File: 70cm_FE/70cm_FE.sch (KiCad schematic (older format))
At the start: 150 parts, among them J2 U.FL, J3 U.FL, J4 U.FL, Q1 2SC3356, Q2 2SC3356, Q3 2SC3356, U1 HT7533-1, U2 74HC14, U3 74HC14, U4 LM393, U5 M68710L

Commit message: Add RF filtering details and other small additions
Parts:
- removed D1: SM4007PL, Diode_SMD:D_SOD-123F, symbol Device:D
- added C1, C2: 100p, Capacitor_SMD:C_0603_1608Metric, symbol Device:C
- added C15, C23: 10p, Capacitor_SMD:C_0603_1608Metric, symbol Device:C
- added C3: 4p7, Capacitor_SMD:C_0402_1005Metric, symbol Device:C
- added C5: DNP, Capacitor_SMD:C_0402_1005Metric, symbol Device:C
- added D1, D3: BAV99, Package_TO_SOT_SMD:SOT-23, symbol Diode:BAV99
- added H5, H6, H7, H8: Tooling hole, 70cm_FE:JLCPCB_ToolingHole, symbol Mechanical:MountingHole
- added JP4, JP7: ~, 70cm_FE:Jumper-3_0402, symbol 70cm_FE:Jumper_3_Bridged12
- added L1, L4: 15n, Inductor_SMD:L_0402_1005Metric, symbol Device:L
- added R1, R2, R26: 100k, Resistor_SMD:R_0402_1005Metric, symbol Device:R
- added R11, R13, R6, R7: DNP, Resistor_SMD:R_0402_1005Metric, symbol Device:R
- added R4: 47, Resistor_SMD:R_0402_1005Metric, symbol Device:R
- added R9: 0, Resistor_SMD:R_0402_1005Metric, symbol Device:R
- C7: renamed from C1; value 1p -> 4p7
- D8: renamed from D7; value BAT54C -> BAS70-05; LCSC (none) -> C77300 (extended)
- L12: renamed from L10; value 23 mm -> 22 mm
- L8: renamed from L7; value 24 mm -> 26 mm
- renumbered C8 to C10, C9 to C11, C14 to C13, C6 to C14, C17 to C16, C7 to C17, C19 to C18, C10 to C19, C11 to C20, C23 to C22, C13 to C24, C15 to C25, C16 to C26, C18 to C27, C25 to C28, C20 to C29, C31 to C30, C26 to C31, C22 to C32, C32 to C33, C28 to C34, C24 to C35, C30 to C36, C27 to C37, C33 to C38, C29 to C39, C2 to C4, C34 to C40, C35 to C41, C36 to C42, C37 to C43, C38 to C44, C39 to C45, C40 to C46, C3 to C6, C4 to C8, C5 to C9, D9 to D10, D10 to D11, D3 to D4, D4 to D5, D5 to D6, D6 to D7, D8 to D9, FL2 to FL1, FL1 to FL2, JP2 to JP1, JP4 to JP2, JP1 to JP3, JP3 to JP5, JP5 to JP6, JP6 to JP8, JP7 to JP9, L11 to L10, L9 to L11, L8 to L13, L3 to L2, L4 to L3, L1 to L5, L2 to L6, L5 to L7, L6 to L9, Q2 to Q1, Q1 to Q2, R11 to R10, R6 to R12, R1 to R14, R10 to R15, R12 to R16, R13 to R17, R14 to R18, R3 to R19, R16 to R20, R7 to R21, R17 to R22, R8 to R23, R9 to R24, R15 to R25, R21 to R27, R18 to R28, R19 to R29, R2 to R3, R22 to R30, R20 to R31, R23 to R32, R24 to R33, R25 to R34, R26 to R35, R27 to R36, R28 to R37, R29 to R38, R30 to R39, R31 to R40, R32 to R41, R33 to R42, R34 to R43, R35 to R44, R36 to R45, R37 to R46, R38 to R47, R39 to R48, R40 to R49, R4 to R5, R41 to R50, R42 to R51, R43 to R52, R44 to R53, R45 to R54, R46 to R55, R47 to R56, R48 to R57, R49 to R58, R50 to R59, R51 to R60, R52 to R61, R53 to R62, R54 to R63, R55 to R64, R56 to R65, R57 to R66, R58 to R67, R59 to R68, R60 to R69, R61 to R70, R5 to R8
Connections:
- net GND: now also C5.2, D1.1 (K), D3.1 (K), D3.2 (A), L4.2, R1.2, R11.2, R13.2, R2.2, R26.2, R4.2, R6.2, R7.2
- net LNA_C: now also C11.1; no longer R10.1
- net LNA_OUT: now also JP4.1 (A); no longer JP2.2 (C)
- net PIN_RXRF: now also JP7.2 (C), R26.1; no longer C22.1
- net RX: now also C2.2, R2.1; no longer JP1.2 (C)
- net RXSAW_IN: no longer R5.1
- net RXSAW_OUT: no longer R3.1
- net TX: now also C1.2, R1.1; no longer C7.1, JP3.2 (C)
- net TXSAW_bypass: now also JP3.1 (A); no longer JP3.3 (B)
- net TXSAW_in: now also JP3.3 (B); no longer JP3.1 (A), R14.1
- net TXSAW_out: no longer R19.1
- net V_in: now also D1.2 (A), D1.3 (K)
- net at R10.2: now also JP2.2 (C), R5.1, R7.1; no longer C11.1
- net TX_filtered: now reaches JP5.2 (C), JP6.2 (C)
- net TX_filtered: now also R19.1
- new net: JP4.2 (C), R10.1, R13.1
- new net: C2.1, JP1.2 (C), R3.1
- new net: JP3.2 (C), R11.1, R14.1, R9.1
- new net: C1.1, C3.1, L1.1
- new net: C5.1, C7.1, L1.2, R6.1, R9.2
- new net: C15.1, C23.2, D3.3 (K), L4.1
- new net: C3.2, R4.1
- new net LNA_IN: C22.1, JP7.1 (A)
- new net LNA_bypass_in: C23.1, JP7.3 (B)
- new net LNA_bypass_out: C15.2, JP4.3 (B)
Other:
- note added: "Control logic.\nDiodes are used for sequencing delays:\n\nWhen TX_ON goes high, LNA turns off first.\nAfter some delay, driver stage and PIN switch are turned on.\nPA bias starts ramping up at roughly the same time.\n\nWhen TX_ON goes low, PA bias starts ramping down first.\nAfter some delay, driver stage and PIN switch are turned off.\nAfter a bit more delay, LNA is turned on.\n\nOvertemperature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"
- note added: "Driver stage\n"
- note added: "For better power handling, series coils are replaced\nwith high impedance microstrip lines."
- note added: "LNA bypass branch also includes diodes\nto protect the receiver."
- note added: "Low-noise amplifier"
- note added: "Optional attenuator"
- note added: "Optional matching components"
- note added: "TODO: Maybe include a second harmonic notch in the filter.\nNow the filter attenuates by 25 dB and the hybrid outputs max. -25 dBc.\nThe resulting 50 dB rejection is not enough."
- note added: "This filter attenuates harmonic mixing products\nfrom the SDR while terminating them in a matched load.\nCapacitance of the detector diode forms a part of the output capacitor."
- note removed: "Control logic.\nDiodes can be used for sequencing delays."
- note removed: "For better power handling, some coils are replaced\nwith long, thin microstrip lines.\nWorst-case power loss in 15 nH 0402 coil with Q=20\nfrom JLC basic series could have been around 0.5 W.\n"
- note removed: "Here could be some filtering,\nalso for harmonics of the TX drive"
- note removed: "TODO: LNA bypass jumpers.\nShould the bypass branch include\nprotection diodes or not?"
- moved on the sheet: C10, C11, C14, C17, C19, C20, C24, C25, C26, C27, C28, C29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

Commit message: Do some layout for 70 cm frontend
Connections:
- net DET_COMP+: now also U4.5 (+); no longer U4.3 (+)
- net DET_COMP-: now also U4.6 (_); no longer U4.2 (-)
- net DET_COMPout: now also U4.7; no longer U4.1
- net DET_REF: now also D8.1; no longer D8.2
- net DET_RF: now also D8.2; no longer D8.1
- net TempHysteresis: now also U4.3 (+); no longer U4.5 (+)
- net TempLimit: now also U4.2 (-); no longer U4.6 (_)
- net ~OverTemp~: now also U4.1; no longer U4.7
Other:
- moved on the sheet: U4A, U4B
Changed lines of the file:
@@
 Connection ~ 13650 800
 $Comp
-L Diode:BAT54C D8
-U 1 1 5FB57769
-P 12050 1100
-F 0 "D8" V 12004 1188 50  0000 L CNN
-F 1 "BAS70-05" V 12095 1188 50  0000 L CNN
-F 2 "Package_TO_SOT_SMD:SOT-23" H 12125 1225 50  0001 L CNN
-F 3 "https://datasheet.lcsc.com/szlcsc/Changjiang-Electronics-Tech-CJ-BAS70-05_C77300.pdf" H 11970 1100 50  0001 C CNN
-F 4 "C77300 (extended)" V 12050 1100 50  0001 C CNN "LCSC"
-	1    12050 1100
-	0    1    1    0
-$EndComp
-$Comp
 L Device:R R46
 U 1 1 5FB5F3A4
@@
 L Comparator:LM393 U4
 U 2 1 5FAC7E0B
-P 13150 2400
-F 0 "U4" H 13150 2767 50  0000 C CNN
-F 1 "LM393" H 13150 2676 50  0000 C CNN
-F 2 "Package_SO:SOIC-8_3.9x4.9mm_P1.27mm" H 13150 2400 50  0001 C CNN
-F 3 "https://datasheet.lcsc.com/szlcsc/ON-Semicon-ON-LM393DR2G_C7955.pdf" H 13150 2400 50  0001 C CNN
-F 4 "C7955" H 13150 2400 50  0001 C CNN "LCSC"
-	2    13150 2400
-	1    0    0    -1
-$EndComp
-$Comp
-L Comparator:LM393 U4
-U 1 1 5FAC6D87
 P 13150 1100
 F 0 "U4" H 13150 1467 50  0000 C CNN
@@
 F 3 "https://datasheet.lcsc.com/szlcsc/ON-Semicon-ON-LM393DR2G_C7955.pdf" H 13150 1100 50  0001 C CNN
 F 4 "C7955" H 13150 1100 50  0001 C CNN "LCSC"
-	1    13150 1100
+	2    13150 1100
+	1    0    0    -1
+$EndComp
+$Comp
+L Comparator:LM393 U4
+U 1 1 5FAC6D87
+P 13150 2400
+F 0 "U4" H 13150 2767 50  0000 C CNN
+F 1 "LM393" H 13150 2676 50  0000 C CNN
+F 2 "Package_SO:SOIC-8_3.9x4.9mm_P1.27mm" H 13150 2400 50  0001 C CNN
+F 3 "https://datasheet.lcsc.com/szlcsc/ON-Semicon-ON-LM393DR2G_C7955.pdf" H 13150 2400 50  0001 C CNN
+F 4 "C7955" H 13150 2400 50  0001 C CNN "LCSC"
+	1    13150 2400
 	1    0    0    -1
 $EndComp
@@
 Text Notes 4550 7450 0    50   ~ 0
 Low-noise amplifier
+$Comp
+L Diode:BAT54C D8
+U 1 1 5FB57769
+P 12050 1100
+F 0 "D8" V 12004 1188 50  0000 L CNN
+F 1 "BAS70-05" V 12095 1188 50  0000 L CNN
+F 2 "Package_TO_SOT_SMD:SOT-23" H 12125 1225 50  0001 L CNN
+F 3 "https://datasheet.lcsc.com/szlcsc/Changjiang-Electronics-Tech-CJ-BAS70-05_C77300.pdf" H 11970 1100 50  0001 C CNN
+F 4 "C77300 (extended)" V 12050 1100 50  0001 C CNN "LCSC"
+	1    12050 1100
+	0    1    -1   0
+$EndComp
 $EndSCHEMATC

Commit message: More 70 cm frontend layout
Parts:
- added C3: 1u, Capacitor_SMD:C_0402_1005Metric, symbol Device:C
- added C33, C5: 10u, Capacitor_SMD:C_1206_3216Metric, symbol Device:C
- added Q1: 2SC3356, Package_TO_SOT_SMD:SOT-23, symbol Device:Q_NPN_BEC
- added R16: 47, Resistor_SMD:R_0402_1005Metric, symbol Device:R
- added R18: 100, Resistor_SMD:R_0402_1005Metric, symbol Device:R
- added R73: 0, Resistor_SMD:R_0603_1608Metric, symbol Device:R
- C25: renamed from C24; value 10p -> 10p (?); footprint Capacitor_SMD:C_0603_1608Metric -> Capacitor_SMD:C_0402_1005Metric
- C38: renamed from C35; value 100n -> 1u; LCSC C1525 -> C52923
- R21: renamed from R17; value 68 -> 100
- renumbered C8 to C10, C10 to C11, C9 to C12, C11 to C13, C12 to C14, C14 to C15, C15 to C16, C13 to C18, C16 to C19, C19 to C20, C20 to C21, C18 to C22, C22 to C23, C23 to C24, C25 to C26, C21 to C27, C26 to C28, C27 to C29, C28 to C30, C29 to C31, C30 to C32, C31 to C34, C32 to C35, C33 to C36, C34 to C37, C36 to C39, C3 to C4, C37 to C40, C38 to C41, C39 to C42, C40 to C43, C41 to C44, C42 to C45, C43 to C46, C44 to C47, C45 to C48, C46 to C49, C5 to C6, C4 to C7, C7 to C8, C6 to C9, L4 to L3, L3 to L4, Q1 to Q2, Q2 to Q3, Q3 to Q4, R8 to R15, R15 to R17, R16 to R19, R19 to R20, R18 to R22, R20 to R23, R21 to R24, R23 to R25, R24 to R26, R22 to R27, R25 to R28, R26 to R29, R28 to R30, R29 to R31, R27 to R32, R30 to R33, R32 to R34, R33 to R35, R34 to R36, R35 to R37, R36 to R38, R37 to R39, R38 to R40, R39 to R41, R40 to R42, R41 to R43, R42 to R44, R43 to R45, R44 to R46, R45 to R47, R46 to R48, R47 to R49, R31 to R5, R48 to R50, R49 to R51, R50 to R52, R51 to R53, R52 to R54, R53 to R55, R54 to R56, R55 to R57, R56 to R58, R57 to R59, R5 to R6, R58 to R60, R59 to R61, R60 to R62, R61 to R63, R62 to R64, R63 to R65, R64 to R66, R65 to R67, R66 to R68, R67 to R69, R6 to R7, R68 to R70, R69 to R71, R70 to R72, R7 to R8
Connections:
- net GND: now also C3.2, C33.2, C5.2, R18.2
- net LNA_C: now also Q1.1 (B); no longer C13.1
- net LNA_VCC: now also Q1.3 (C)
- net PA_VDD: now also C33.1
- net V_in: now also R73.1; no longer J1.1 (Pin_1)
- net REG_GND: now reaches R17.1, R19.2, U1.1 (GND)
- net REG_in: now reaches C12.1, R15.2, U1.2 (VIN)
- new net: Q1.2 (E), R16.1, R18.1
- new net: C13.1, R16.2
- new net V_in1: C3.1, C5.1, J1.1 (Pin_1), R73.2
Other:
- moved on the sheet: C12, C13, C14, C18, C19, C22, C27, C35, C7, C9, D1, L2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

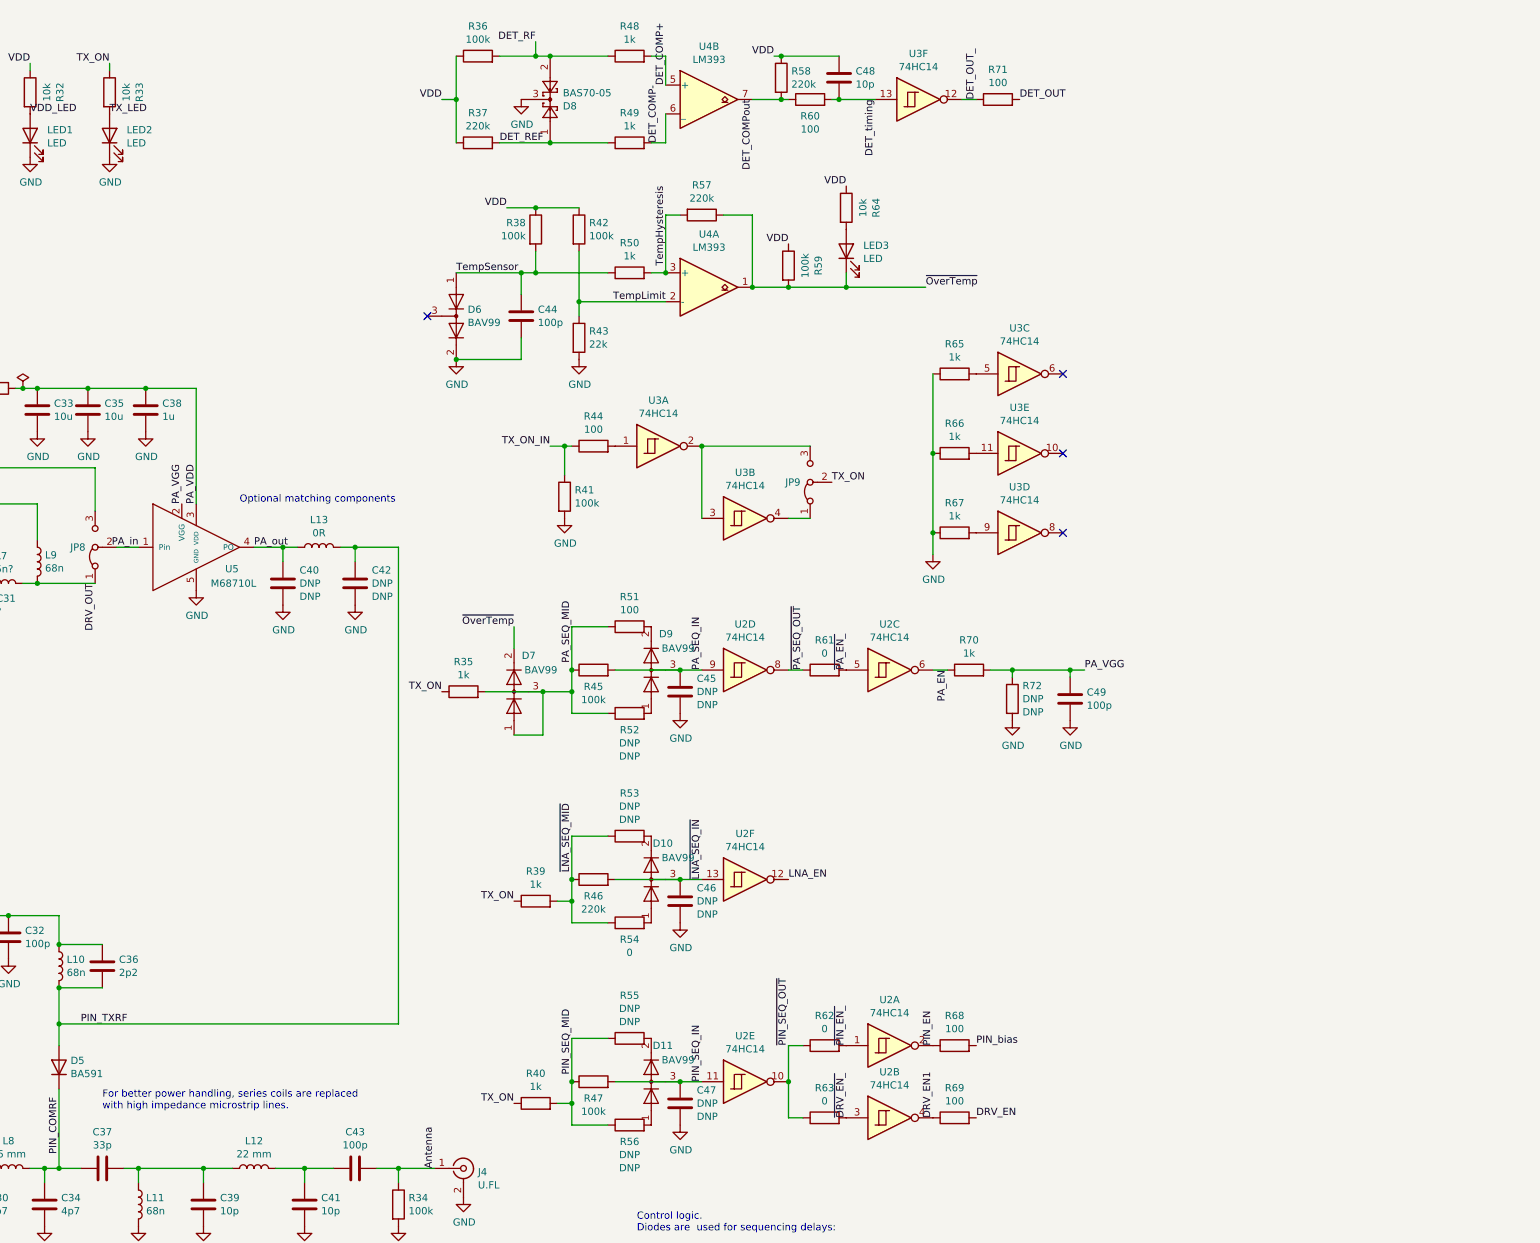
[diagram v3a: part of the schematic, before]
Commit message: Change the order of inverters for better layout
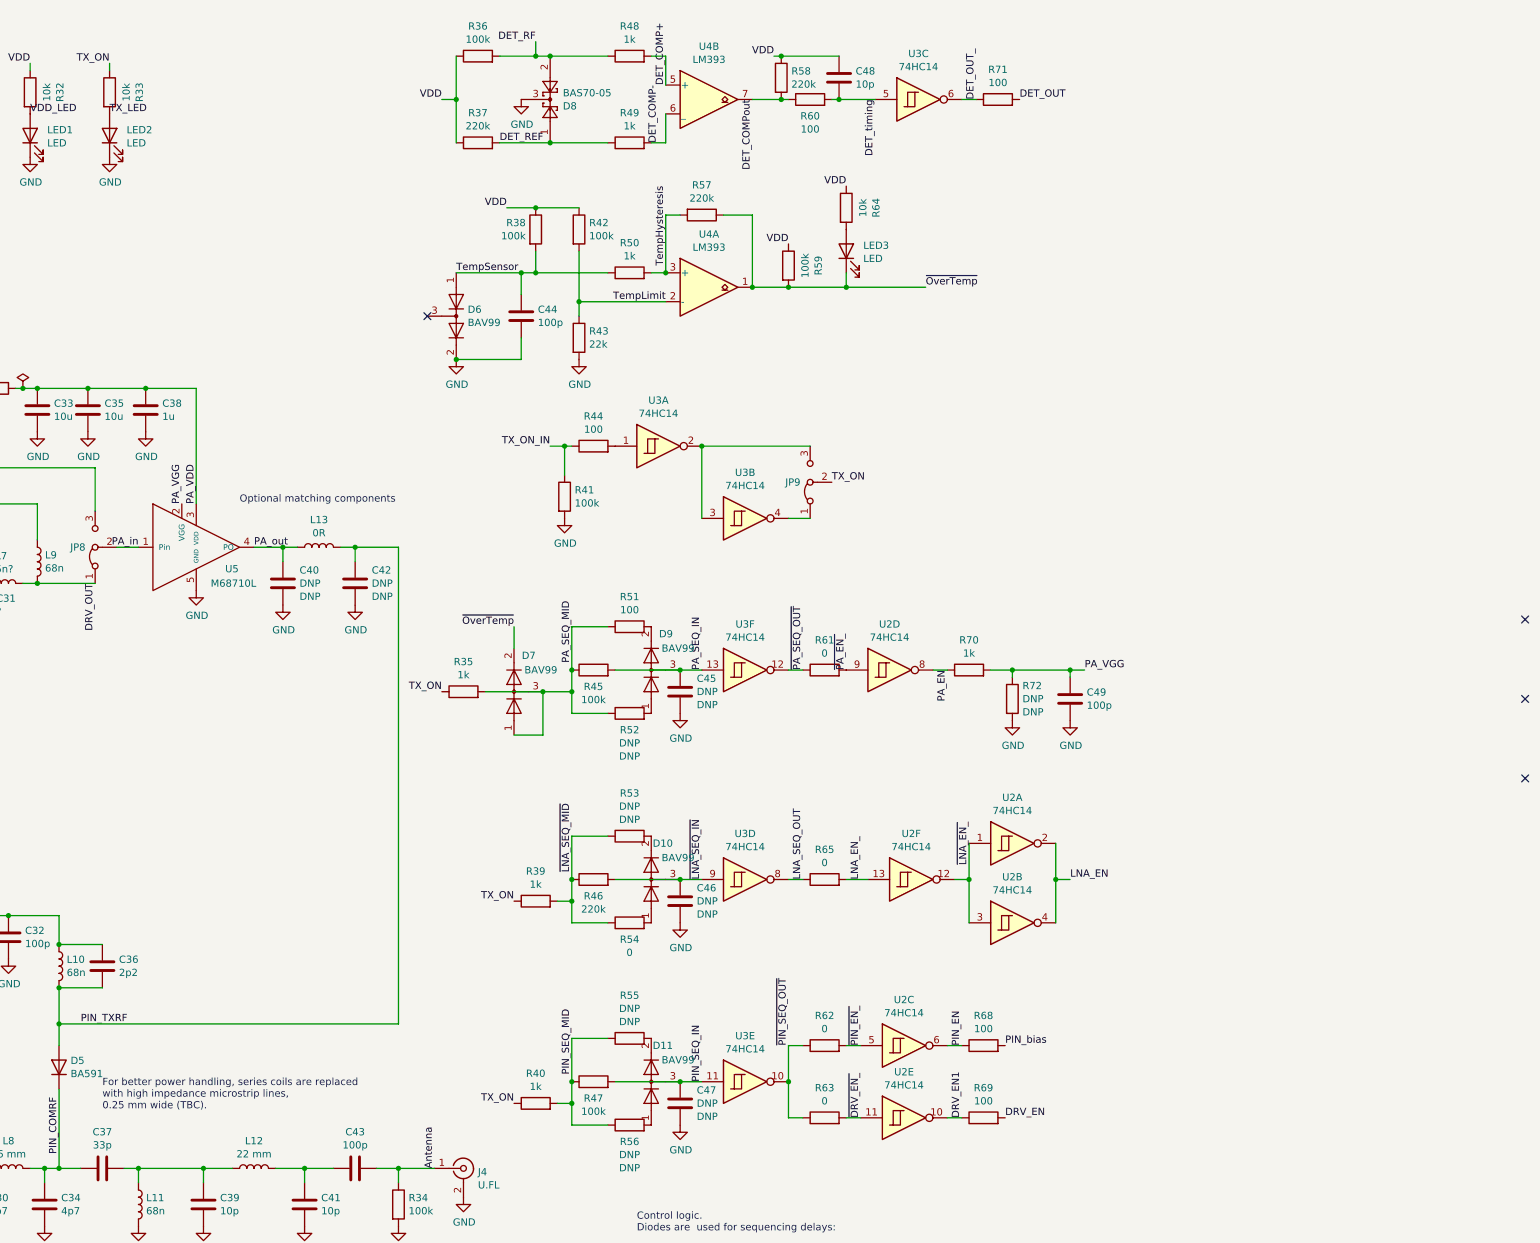
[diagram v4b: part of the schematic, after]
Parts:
- removed R66, R67: 1k, Resistor_SMD:R_0402_1005Metric, symbol Device:R
- R65: value 1k -> 0
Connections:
- net DET_OUT_: now also U3.6; no longer U3.12
- net DET_timing: now also U3.5; no longer U3.13
- net DRV_EN1: now also U2.10; no longer U2.4
- net GND: no longer R65.1
- net LNA_EN: now also U2.2, U2.4; no longer U2.12
- net PA_EN: now also U2.8; no longer U2.6
- net PA_SEQ_IN: now also U3.13; no longer U2.9
- net PIN_EN: now also U2.6; no longer U2.2
- net PIN_SEQ_IN: now also U3.11; no longer U2.11
- net ~DRV_EN_~: now also U2.11; no longer U2.3
- net ~LNA_SEQ_IN~: now also U3.9; no longer U2.13
- net ~PA_EN_~: now also U2.9; no longer U2.5
- net ~PA_SEQ_OUT~: now also U3.12; no longer U2.8
- net ~PIN_EN_~: now also U2.5; no longer U2.1
- net ~PIN_SEQ_OUT~: now also U3.10; no longer U2.10
- net LNA_EN_: now reaches R65.2
- net LNA_EN_: now also U2.13; no longer U3.5
- net LNA_SEQ_OUT: now reaches U3.8
- net LNA_SEQ_OUT: now also R65.1
- new net ~LNA_EN_~: U2.1, U2.12, U2.3
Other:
- note added: "For better power handling, series coils are replaced\nwith high impedance microstrip lines,\n0.25 mm wide (TBC)."
- note removed: "For better power handling, series coils are replaced\nwith high impedance microstrip lines."
- moved on the sheet: R65, R68, R69, U2A, U2B, U2C, U2D, U2E, U2F, U3C, U3D, U3E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
